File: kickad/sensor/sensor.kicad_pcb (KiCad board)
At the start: 2 copper layers, 188.6 x 130 mm, 27 parts, among them J3 trackball, U2 PMW3610, U4 MCP1700x-180xxTT

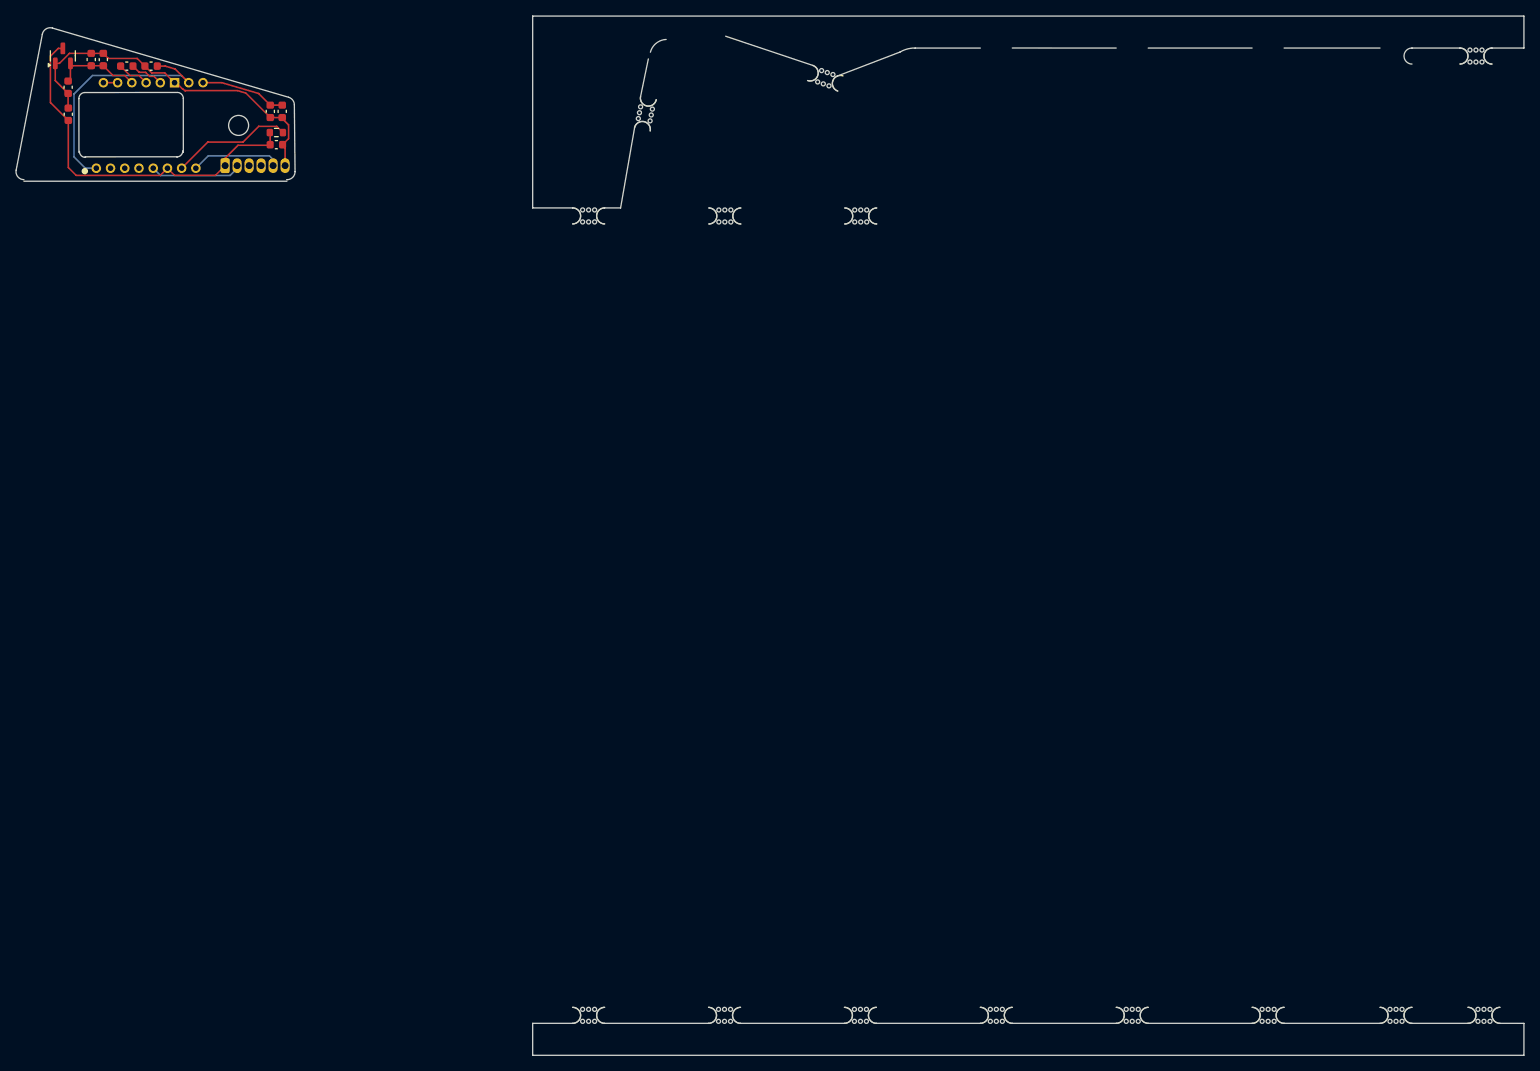
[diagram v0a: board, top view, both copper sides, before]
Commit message: Reworking the sensor PCB
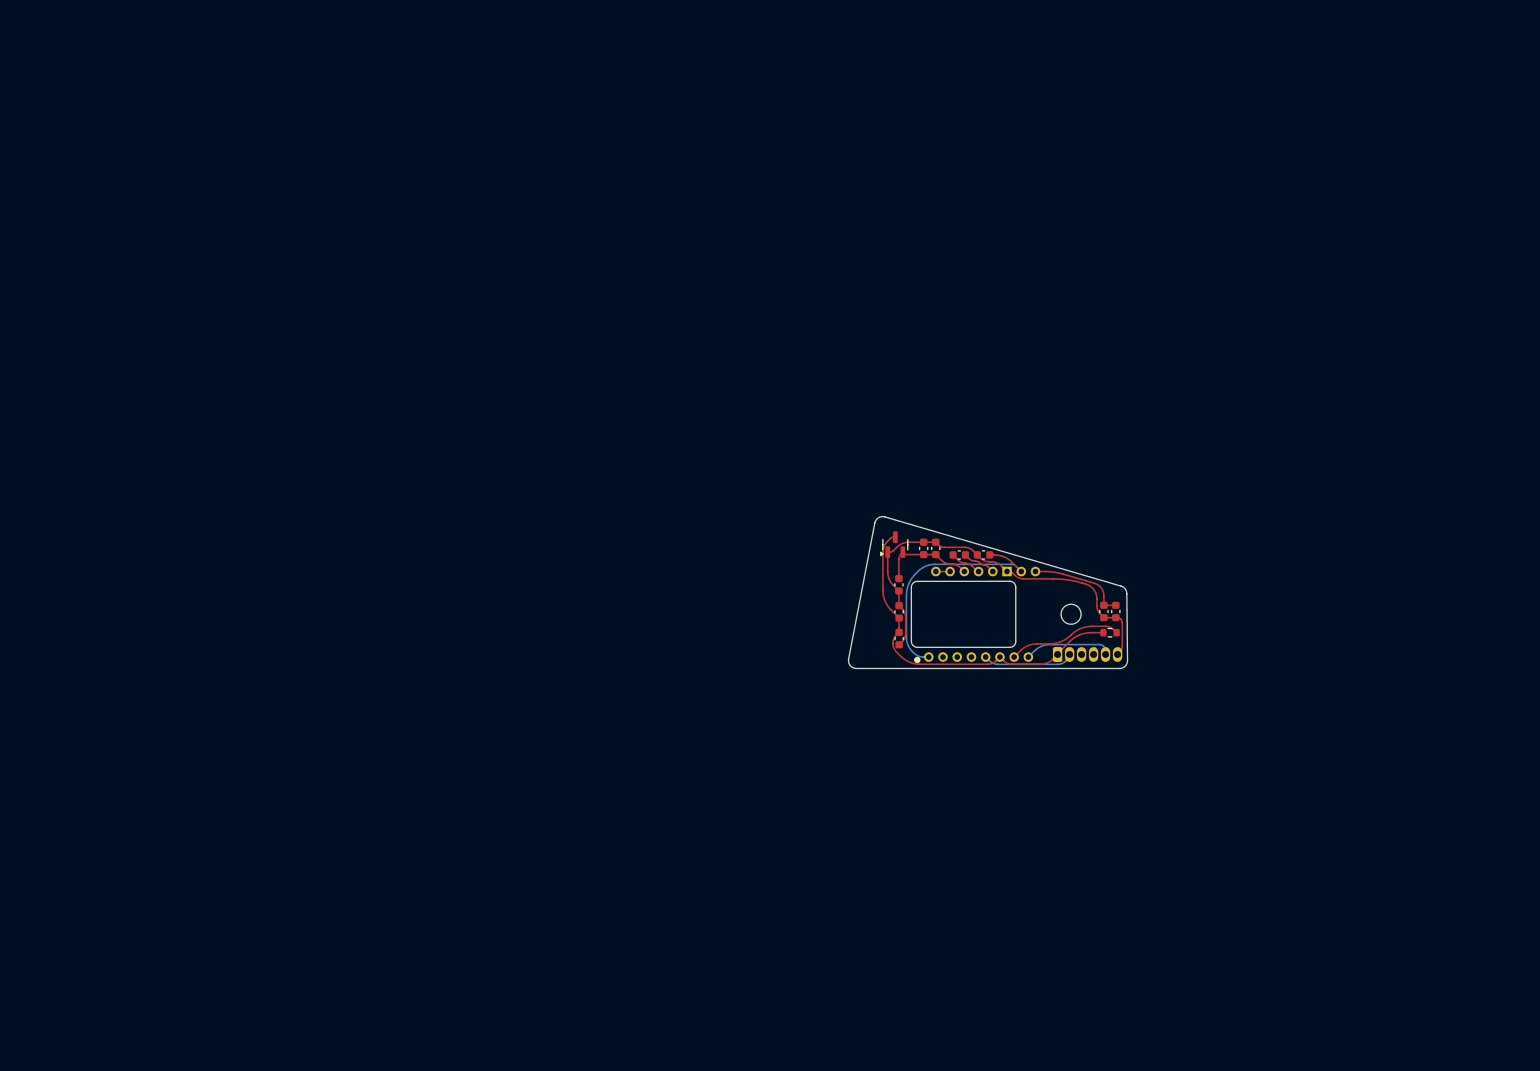
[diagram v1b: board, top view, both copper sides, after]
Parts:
- removed mouse-bite-2mm-slot (x14): VAL**, Panelization:mouse-bite-2mm-slot
- moved C8 121.6 mm to (151.5, 100.5)
- moved R1 121.6 mm to (152.2, 103.1)
- moved C9 121.6 mm to (152.9, 100.5)
- moved C10 121.1 mm to (125.8, 97.1)
- moved C11 121.1 mm to (125.8, 100.5)
- moved C3 120.8 mm to (130.4, 92.6)
- moved C6 120.8 mm to (133.4, 93.4)
- moved U1 120.8 mm to (125.4, 92.1)
- moved C1 120.8 mm to (136.4, 93.4)
- moved C2 120.8 mm to (128.9, 92.6)
- moved J3 120.8 mm to (145.7, 105.9)
- moved U2 120.8 mm to (133.8, 100.8)
- moved C7 99.4 mm to (125.8, 103.9), turned to -90 degrees
- renumbered U4 to U1
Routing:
- net SDIO: track 0.00 -> 18.3 mm
- net SCLK: track 0.00 -> 17.8 mm
- net GND: track 46.2 -> 51.8 mm
- net 3.3v: track 46.9 -> 44.2 mm
- net Net-(U2-VCP): track 10.7 -> 12.3 mm
- net +1V8: track 11.0 -> 12.1 mm
- net Net-(U2-NRESET): track 15.2 -> 14.2 mm
- net Net-(U2-+VCSEL): track 31.6 -> 31.0 mm
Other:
- board size 188.6 x 130 mm -> 34.9 x 19 mm
- copper layers 2 -> 4

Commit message: Releasing all the gerbers
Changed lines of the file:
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@@
 	)
 	(segment
-		(start 136.022059 94.496042)
+		(start 136.022155 94.496138)
 		(end 135.964009 94.437992)
 		(width 0.2)
@@
 	)
 	(arc
-		(start 136.022059 94.496042)
-		(mid 136.237441 94.639956)
+		(start 136.022155 94.496138)
+		(mid 136.237431 94.639981)
 		(end 136.491501 94.690492)
 		(width 0.2)
@@
 	(segment
 		(start 125.065 104.423007)
-		(end 125.065 104.486848)
+		(end 125.065 104.844371)
 		(width 0.2)
 		(layer "F.Cu")
@@
 	(segment
 		(start 126.057591 106.091287)
-		(end 125.497641 105.531337)
-		(width 0.2)
-		(layer "F.Cu")
-		(net 5)
-	)
-	(segment
-		(start 124.365891 91.740586)
+		(end 125.244834 105.27853)
+		(width 0.2)
+		(layer "F.Cu")
+		(net 5)
+	)
+	(segment
+		(start 124.156395 91.950081)
 		(end 124.754187 91.352291)
 		(width 0.2)
@@
 	)
 	(segment
-		(start 123.817418 93.06472)
+		(start 123.817418 92.768443)
 		(end 123.817418 97.853757)
 		(width 0.2)
@@
 	)
 	(arc
-		(start 125.065 104.486848)
-		(mid 125.177439 105.052121)
-		(end 125.497641 105.531337)
+		(start 125.065 104.844371)
+		(mid 125.111737 105.079336)
+		(end 125.244834 105.27853)
 		(width 0.2)
 		(layer "F.Cu")
@@
 	)
 	(arc
-		(start 124.365891 91.740586)
-		(mid 123.959961 92.348104)
-		(end 123.817418 93.06472)
-		(width 0.2)
-		(layer "F.Cu")
+		(start 124.156395 91.950081)
+		(mid 123.905515 92.325549)
+		(end 123.817418 92.768443)
+		(width 0.2)
+		(layer "F.Cu")
